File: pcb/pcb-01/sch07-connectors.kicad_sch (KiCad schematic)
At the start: 0 parts

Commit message: pcb: capture SCH-04..07, full-project ERC clean
Parallel agent capture of the remaining blocks: SCH-04 ESP32-C6 (full GPIO
map, boot straps, USB chain with TPD2EUSB30 on the connector side of the
22R), SCH-05 permission + watchdog (both '1G74s with the review-fixed /PRE
topologies, six-BAT54H wired-OR, TPS3435 pinout C, separate 100R heartbeat
feeds), SCH-06 analog tach (TPS7A16 protected rail with 10 nF DELAY, LM2907
with grounded CP1 and emitter load, TLV1701 trip stage with C2 DNP ladder),
SCH-07 connectors J1-J8 + 28 test points + DNP input-fuse footprint.

ERC: 0 errors after PWR_FLAGs on VM24/AGND/PGND/TACH_LDO_IN and demoting
the MCF's duplicate OUTx/VM/PGND pins to passive. Konnect never refreshes a
sheet's embedded lib_symbols copy (delete + re-add reuses the stale def), so
that one fix was a keyword-only text edit of three pin types, verified by
kicad-cli's full parse. Remaining 41 warnings are two benign classes:
local+global same-name labels (our labeling convention) and embedded-vs-
library symbol formatting drift.

Vendored Konnect agents re-pinned from dead claude-sonnet-4-20250514 to
claude-sonnet-5.
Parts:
- added F1: DNP - bridge, Fuse:Fuse_1206_3216Metric, symbol Device:Fuse
- added J1: POWER, Connector_Molex:Molex_Micro-Fit_3.0_43045-0200_2x01_P3.00mm_Horizontal, symbol Connector_Generic:Conn_01x02
- added J2: MOTOR, Connector_Molex:Molex_Micro-Fit_3.0_43650-0300_1x03_P3.00mm_Horizontal, symbol Connector_Generic:Conn_01x03
- added J3: HALL, Connector_JST:JST_PH_B3B-PH-K_1x03_P2.00mm_Vertical, symbol Connector_Generic:Conn_01x03
- added J4: TEMP, Connector_JST:JST_PH_B2B-PH-K_1x02_P2.00mm_Vertical, symbol Connector_Generic:Conn_01x02
- added J5: I2C, Connector_JST:JST_SH_BM04B-SRSS-TB_1x04-1MP_P1.00mm_Vertical, symbol Connector_Generic:Conn_01x04
- added J6: USB-C, Connector_USB:USB_C_Receptacle_GCT_USB4105-xx-A_16P_TopMnt_Horizontal, symbol Connector:USB_C_Receptacle_USB2.0_16P
- added J7: PROGRAM, Connector:Tag-Connect_TC2030-IDC-NL_2x03_P1.27mm_Vertical, symbol Connector_Generic:Conn_02x03_Odd_Even
- added J8: DNP 2x5 1.27mm, Connector_PinHeader_1.27mm:PinHeader_2x05_P1.27mm_Vertical, symbol Connector_Generic:Conn_02x05_Odd_Even
- added R55, R56: 5.1k, Resistor_SMD:R_0402_1005Metric, symbol Device:R
- added R57, R58: 100k, Resistor_SMD:R_0402_1005Metric, symbol Device:R
- added TP1: RAW24, TestPoint:TestPoint_Pad_D1.5mm, symbol Connector:TestPoint
- added TP10: U5_CLR_OR, TestPoint:TestPoint_Pad_D1.5mm, symbol Connector:TestPoint
- added TP11: U5_Q, TestPoint:TestPoint_Pad_D1.5mm, symbol Connector:TestPoint
- added TP12: DRVOFF, TestPoint:TestPoint_Pad_D1.5mm, symbol Connector:TestPoint
- added TP13: WD_HEARTBEAT, TestPoint:TestPoint_Pad_D1.5mm, symbol Connector:TestPoint
- added TP14: WDO, TestPoint:TestPoint_Pad_D1.5mm, symbol Connector:TestPoint
- added TP15: WD_MR, TestPoint:TestPoint_Pad_D1.5mm, symbol Connector:TestPoint
- added TP16: MCF_EXT_WD, TestPoint:TestPoint_Pad_D1.5mm, symbol Connector:TestPoint
- added TP17: NFAULT, TestPoint:TestPoint_Pad_D1.5mm, symbol Connector:TestPoint
- added TP18: SDA, TestPoint:TestPoint_Pad_D1.5mm, symbol Connector:TestPoint
- added TP19: SCL, TestPoint:TestPoint_Pad_D1.5mm, symbol Connector:TestPoint
- added TP2: VM24, TestPoint:TestPoint_Pad_D1.5mm, symbol Connector:TestPoint
- added TP20: FG, TestPoint:TestPoint_Pad_D1.5mm, symbol Connector:TestPoint
- added TP21: HALL_TACH, TestPoint:TestPoint_Pad_D1.5mm, symbol Connector:TestPoint
- added TP22: VTACH, TestPoint:TestPoint_Pad_D1.5mm, symbol Connector:TestPoint
- added TP23: VREF, TestPoint:TestPoint_Pad_D1.5mm, symbol Connector:TestPoint
- added TP24: OVERSPEED_N, TestPoint:TestPoint_Pad_D1.5mm, symbol Connector:TestPoint
- added TP25: VBUS_SENSE, TestPoint:TestPoint_Pad_D1.5mm, symbol Connector:TestPoint
- added TP26, TP28, TP4: AGND, TestPoint:TestPoint_Pad_D1.5mm, symbol Connector:TestPoint
- added TP27, TP3: PGND, TestPoint:TestPoint_Pad_D1.5mm, symbol Connector:TestPoint
- added TP5: 3V3, TestPoint:TestPoint_Pad_D1.5mm, symbol Connector:TestPoint
- added TP6: +12V_TACH, TestPoint:TestPoint_Pad_D1.5mm, symbol Connector:TestPoint
- added TP7: MCF_AVDD, TestPoint:TestPoint_Pad_D1.5mm, symbol Connector:TestPoint
- added TP8: MCF_DVDD, TestPoint:TestPoint_Pad_D1.5mm, symbol Connector:TestPoint
- added TP9: PGOOD, TestPoint:TestPoint_Pad_D1.5mm, symbol Connector:TestPoint
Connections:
- new net +12V_TACH: J8.4 (Pin_4), TP6.1
- new net 3V3: J3.1 (Pin_1), J5.2 (Pin_2), J7.1 (Pin_1), J8.3 (Pin_3), TP5.1
- new net AGND: J3.3 (Pin_3), J4.2 (Pin_2), J5.1 (Pin_1), J6.A1 (GND), J6.A12 (GND), J6.B1 (GND), J6.B12 (GND), J6.SH (SHIELD), J7.6 (Pin_6), J8.10 (Pin_10), R55.2, R56.2, R58.2, TP26.1, TP28.1, TP4.1
- new net CC1: J6.A5 (CC1), R55.1
- new net CC2: J6.B5 (CC2), R56.1
- new net DRVOFF: J8.5 (Pin_5), TP12.1
- new net ESP_BOOT: J7.5 (Pin_5)
- new net ESP_EN: J7.4 (Pin_4)
- new net FG: J8.7 (Pin_7), TP20.1
- new net HALL_TACH: J3.2 (Pin_2), TP21.1
- new net MCF_AVDD: TP7.1
- new net MCF_DVDD: TP8.1
- new net MCF_EXT_WD: TP16.1
- new net NFAULT: J8.8 (Pin_8), TP17.1
- new net OVERSPEED_N: TP24.1
- new net PGND: J1.2 (Pin_2), J8.2 (Pin_2), TP27.1, TP3.1
- new net PGOOD: TP9.1
- new net PHASE_U: J2.1 (Pin_1)
- new net PHASE_V: J2.2 (Pin_2)
- new net PHASE_W: J2.3 (Pin_3)
- new net RAW24: F1.2, TP1.1
- new net RAW24_IN: F1.1, J1.1 (Pin_1)
- new net SCL: J5.4 (Pin_4), TP19.1
- new net SDA: J5.3 (Pin_3), TP18.1
- new net SOX: J8.9 (Pin_9)
- new net SPEED: J8.6 (Pin_6)
- new net TEMP_SENSE: J4.1 (Pin_1)
- new net U5_CLR_OR: TP10.1
- new net U5_Q: TP11.1
- new net UART_RX: J7.3 (Pin_3)
- new net UART_TX: J7.2 (Pin_2)
- new net USB_DM: J6.A7 (D-), J6.B7 (D-)
- new net USB_DP: J6.A6 (D+), J6.B6 (D+)
- new net VBUS: J6.A4 (VBUS), J6.A9 (VBUS), J6.B4 (VBUS), J6.B9 (VBUS), R57.1
- new net VBUS_SENSE: R57.2, R58.1, TP25.1
- new net VM24: J8.1 (Pin_1), TP2.1
- new net VREF: TP23.1
- new net VTACH: TP22.1
- new net WDO: TP14.1
- new net WD_HEARTBEAT: TP13.1
- new net WD_MR: TP15.1
- no-connect marks 0 -> 2
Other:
- note added: "DNP fuse footprint - bridge when unfitted (source fuse lives in the wall box)"

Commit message: pcb: review round 1 fixes — hall pull-up, ground tie, DNP marks, footprints
13-lens board-truth review (netlist as source of truth, spec excluded to
avoid circular validation) found and this commit fixes in the schematic:

- R43 was a 100k pulldown to AGND on HALL_TACH; the DRV5033 is open-drain,
  so the hall line could never go high and the analog overspeed chain could
  never trip. Now 10k pull-up to 3V3 (matching the daughterboard section's
  original intent; the LM2907 spec section contradicted it).
- PGND and AGND had no bridge anywhere (the "wide net tie" was layout-note
  prose only): added NT1 (NetTie-2_SMD_Pad2.0mm) on SCH-03.
- C36-C40 tach filter alternates carried no DNP marking; as captured all six
  caps would be assembled in parallel (~18.5uF, ~12s trip lag). Values now
  say DNP.
- J5 footprint was the vertical BM04B while the BOM ordered the side-entry
  SM04B (mating cable already purchased); footprint corrected.
- U12 TPD2EUSB30 was on SOT-563; the part only exists in DRT 3-pin SOT.
  Now Texas_DRT-3 (stock footprint, cites this exact part).
- R3 PGOOD pull-up moved from VOUT to U3_VCC per TI practice; C17 given a
  rating (22uF 25V X7R).

Spec (docs/electrical.md) updated to match, plus an "Open items from the
2026-07 board-truth review" section for the accepted tradeoffs and firmware
TODOs. bom.csv U12 package corrected. groups.json: C32 reassigned from
dnp_bank to tach (functional filter cap, not an alternate).

ERC: no errors (35 pre-existing same_local_global_label warnings from the
label convention). Board-side sync happens via Update-PCB-from-Schematic.
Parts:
- J5: footprint Connector_JST:JST_SH_BM04B-SRSS-TB_1x04-1MP_P1.00mm_Vertical -> Connector_JST:JST_SH_SM04B-SRSS-TB_1x04-1MP_P1.00mm_Horizontal
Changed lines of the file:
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@@
         (font
           (size 1.27 1.27))))
-    (property "Footprint" "Connector_JST:JST_SH_BM04B-SRSS-TB_1x04-1MP_P1.00mm_Vertical"
+    (property "Footprint" "Connector_JST:JST_SH_SM04B-SRSS-TB_1x04-1MP_P1.00mm_Horizontal"
       (at 160.02 49.53 0)
       (hide yes)

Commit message: pcb: review round 2 — safety-latch decoupling, docs, calibration rationale
Round-2 lenses (fix-verify, placement-physics, calibration math, MCF
register-image audit, completeness critic) confirmed every round-1 fix
end-to-end and found: U5 and U6 — the permission and overspeed latches —
were the only logic ICs without local decoupling (nearest 3V3 cap 13mm from
U5). Added C42/C43 (100nF 0402) on SCH-05. J5's stale MPN field corrected
to SM04B-SRSS-TB(LF)(SN).

Docs: calibration section now states WHY per-unit RV1 trim is mandatory
(LM2907 K = +/-10% => +/-20 RPM untrimmed) and the expected ~+/-10 RPM
threshold scatter (ripple ~= hysteresis) with the C36-C40 bank as the
remedy; open-items gains the MCF register-image capture checklist
(SPEED_MODE/SPEED_RANGE_SEL, ALARM_PIN_EN/OTW_REP, EXT_WDT_* and the
unmapped MAX_SPEED seed), the cold-plug VM ramp analysis (refuted by
bulk-bank physics, bench inrush check stands), and the V2 ESD note for
sensor pigtails/buttons. Verified: 12 thermal vias under U1's pad; zero new
wiring defects in the round-2 sweep; pole count, watchdog timing, trip
math all independently reproduce the documented targets.
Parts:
- J5: MPN BM04B-SRSS-TB -> SM04B-SRSS-TB(LF)(SN)
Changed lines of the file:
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@@
         (font
           (size 1.27 1.27))))
-    (property "MPN" "BM04B-SRSS-TB"
+    (property "MPN" "SM04B-SRSS-TB(LF)(SN)"
       (at 0 0 0)
       (effects

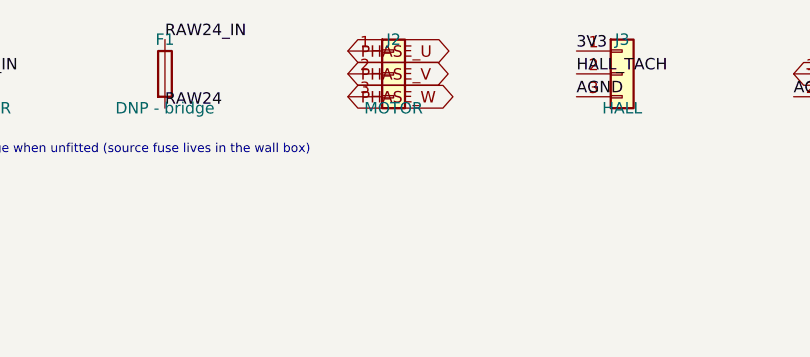
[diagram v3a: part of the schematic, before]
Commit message: pcb: route PCB-01 power, USB, ESP — mid-session checkpoint
L2 AGND plane + PGND island (NT1-only bridge), antenna keepout, phases
to J2 (U/W pins swapped for straight runs), MCF west cluster, input
stage, L3 split VM24/3V3 planes with via-storm distribution, 3V3
regulator, USB fan-out + FS diff pair, ESP power. Net classes actually
persisted to .kicad_pro (setup script had never run). C12/C15 rotated
180 as routing-driven placement fixes. Rationale in electrical.md
"Routing notes"; STATE.md reflects the checkpoint. Remaining: buck
loop, digital fan-out, tach analog, fills, silk sweep.
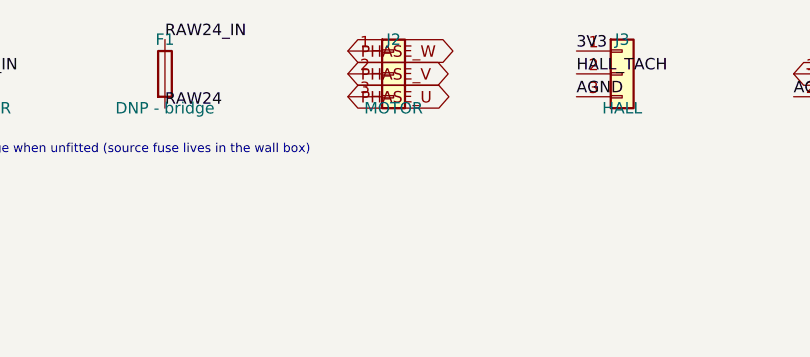
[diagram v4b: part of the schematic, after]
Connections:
- net PHASE_U: now also J2.3 (Pin_3); no longer J2.1 (Pin_1)
- net PHASE_W: now also J2.1 (Pin_1); no longer J2.3 (Pin_3)
